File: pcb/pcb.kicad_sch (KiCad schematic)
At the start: 121 parts, among them J1 Conn_01x06_Pin, SW1 SW_Push_45deg, SW10 SW_Push_45deg, SW11 SW_Push_45deg, SW12 SW_Push_45deg, SW13 SW_Push_45deg, SW14 SW_Push_45deg, SW15 SW_Push_45deg, SW16 SW_Push_45deg, SW17 SW_Push_45deg, SW18 SW_Push_45deg, SW19 SW_Push_45deg, SW2 SW_Push_45deg, SW20 SW_Push_45deg, SW21 SW_Push_45deg, SW22 SW_Push_45deg, SW23 SW_Push_45deg, SW24 SW_Push_45deg, SW25 SW_Push_45deg, SW26 SW_Push_45deg, SW27 SW_Push_45deg, SW28 SW_Push_45deg, SW29 SW_Push_45deg, SW3 SW_Push_45deg, SW30 SW_Push_45deg, SW31 SW_Push_45deg, SW32 SW_Push_45deg, SW33 SW_Push_45deg, SW34 SW_Push_45deg, SW35 SW_Push_45deg, SW36 SW_Push_45deg, SW37 SW_Push_45deg, SW38 SW_Push_45deg, SW39 SW_Push_45deg, SW4 SW_Push_45deg, SW40 SW_Push_45deg, SW41 SW_Push_45deg, SW42 SW_Push_45deg, SW43 SW_Push_45deg, SW44 SW_Push_45deg, SW45 SW_Push_45deg, SW46 SW_Push_45deg, SW47 SW_Push_45deg, SW48 SW_Push_45deg, SW49 SW_Push_45deg, SW5 SW_Push_45deg, SW50 SW_Push_45deg, SW51 SW_Push, SW52 SW_Push, SW6 SW_Push_45deg, SW7 SW_Push_45deg, SW8 SW_Push_45deg, SW9 SW_Push_45deg, U1 STM32U575RGTxQ

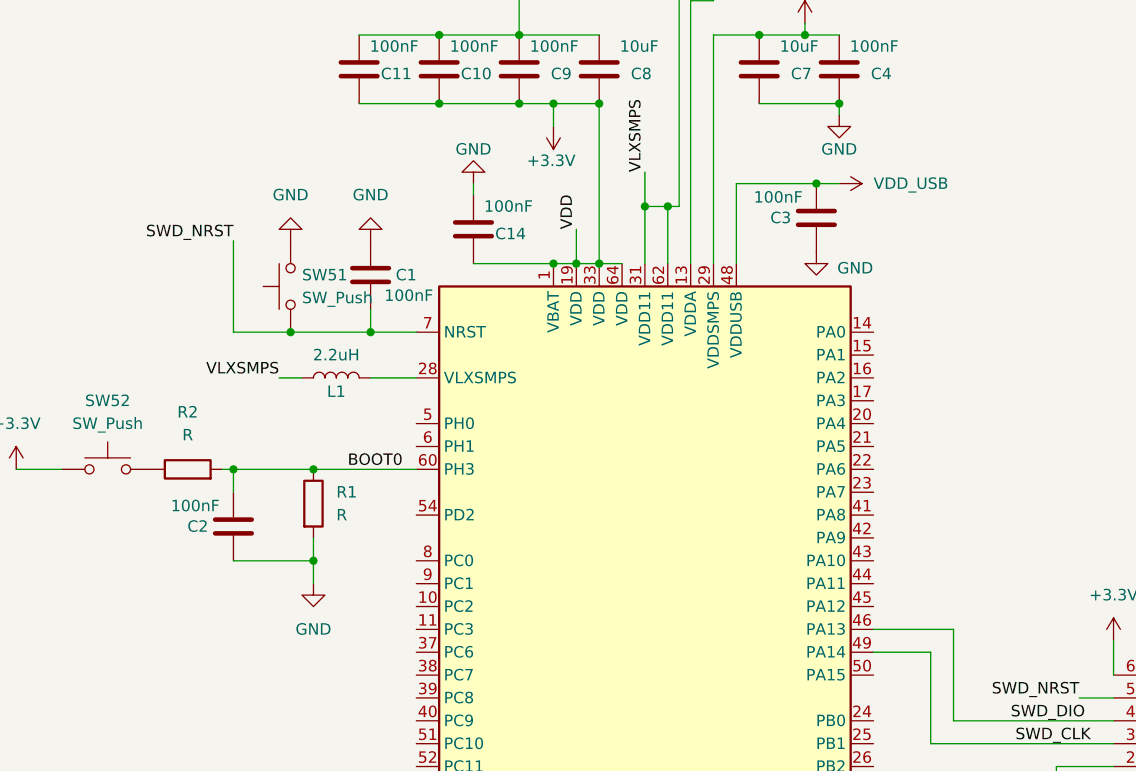
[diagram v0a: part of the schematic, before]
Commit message: [Hardware] Add R1 and R2 values, tied VDDUSB to VDD correctly
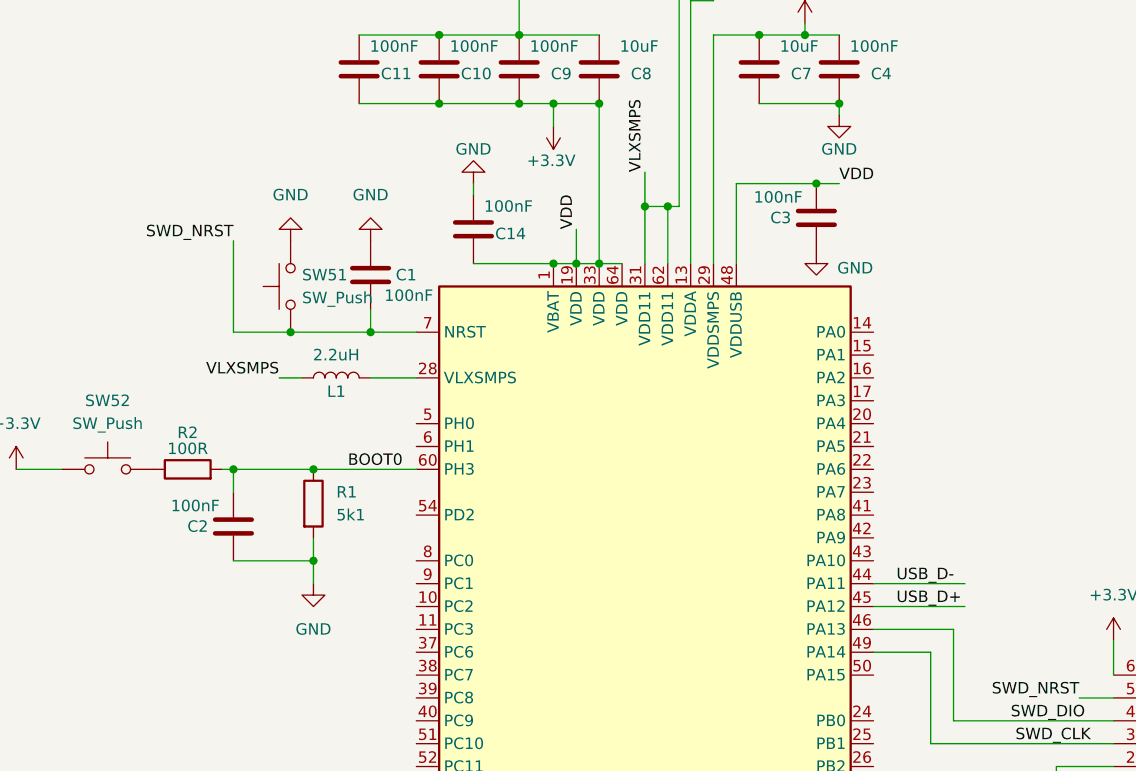
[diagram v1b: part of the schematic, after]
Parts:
- R1: value R -> 5k1
- R2: value R -> 100R
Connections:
- net VDD_USB is gone; now on net +3.3V: C3.2, U1.48 (VDDUSB)
- net USB_D-: now reaches U1.44 (PA11)
- net USB_D+: now reaches U1.45 (PA12)
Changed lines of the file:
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@@
 	(wire
 		(pts
+			(xy 226.06 148.59) (xy 236.22 148.59)
+		)
+		(stroke
+			(width 0)
+			(type default)
+		)
+	)
+	(wire
+		(pts
 			(xy 95.25 88.9) (xy 109.22 88.9)
 		)
@@
 	(wire
 		(pts
+			(xy 226.06 146.05) (xy 236.22 146.05)
+		)
+		(stroke
+			(width 0)
+			(type default)
+		)
+	)
+	(wire
+		(pts
 			(xy 24.13 195.58) (xy 39.37 195.58)
 		)
@@
 		)
 	)
+	(label "USB_D-"
+		(at 228.6 146.05 0)
+		(effects
+			(font
+				(size 1.27 1.27)
+			)
+			(justify left bottom)
+		)
+	)
 	(label "BOOT0"
 		(at 167.64 133.35 0)
@@
 		)
 	)
+	(label "USB_D+"
+		(at 228.6 148.59 0)
+		(effects
+			(font
+				(size 1.27 1.27)
+			)
+			(justify left bottom)
+		)
+	)
 	(label "VLXSMPS"
 		(at 160.02 123.19 180)
@@
 		)
 	)
+	(label "VDD"
+		(at 222.25 101.6 0)
+		(effects
+			(font
+				(size 1.27 1.27)
+			)
+			(justify left bottom)
+		)
+	)
 	(label "SWD_NRST"
 		(at 154.94 107.95 180)
@@
 			)
 		)
-		(property "Value" "R"
+		(property "Value" "5k1"
 			(at 166.37 138.4299 0)
 			(effects
@@
 	)
 	(symbol
-		(lib_id "power:VDD")
-		(at 222.25 101.6 270)
-		(unit 1)
-		(exclude_from_sim no)
-		(in_bom yes)
-		(on_board yes)
-		(dnp no)
-		(fields_autoplaced yes)
-		(property "Reference" "#PWR08"
-			(at 218.44 101.6 0)
-			(effects
-				(font
-					(size 1.27 1.27)
-				)
-				(hide yes)
-			)
-		)
-		(property "Value" "VDD_USB"
-			(at 226.06 101.5999 90)
-			(effects
-				(font
-					(size 1.27 1.27)
-				)
-				(justify left)
-			)
-		)
-		(property "Footprint" ""
-			(at 222.25 101.6 0)
-			(effects
-				(font
-					(size 1.27 1.27)
-				)
-				(hide yes)
-			)
-		)
-		(property "Datasheet" ""
-			(at 222.25 101.6 0)
-			(effects
-				(font
-					(size 1.27 1.27)
-				)
-				(hide yes)
-			)
-		)
-		(property "Description" "Power symbol creates a global label with name \"VDD\""
-			(at 222.25 101.6 0)
-			(effects
-				(font
-					(size 1.27 1.27)
-				)
-				(hide yes)
-			)
-		)
-		(pin "1"
-		)
-		(instances
-			(project ""
-				(path "/f2ec7380-d5e2-4be5-b548-cc5c4c4a2ed6"
-					(reference "#PWR08")
-					(unit 1)
-				)
-			)
-		)
-	)
-	(symbol
 		(lib_id "Switch:SW_Push_45deg")
 		(at 106.68 100.33 0)
@@
 		(on_board yes)
 		(dnp no)
-		(fields_autoplaced yes)
 		(property "Reference" "R2"
-			(at 149.86 127 90)
+			(at 149.86 129.286 90)
 			(effects
 				(font
@@
 			)
 		)
-		(property "Value" "R"
-			(at 149.86 129.54 90)
+		(property "Value" "100R"
+			(at 149.86 131.064 90)
 			(effects
 				(font

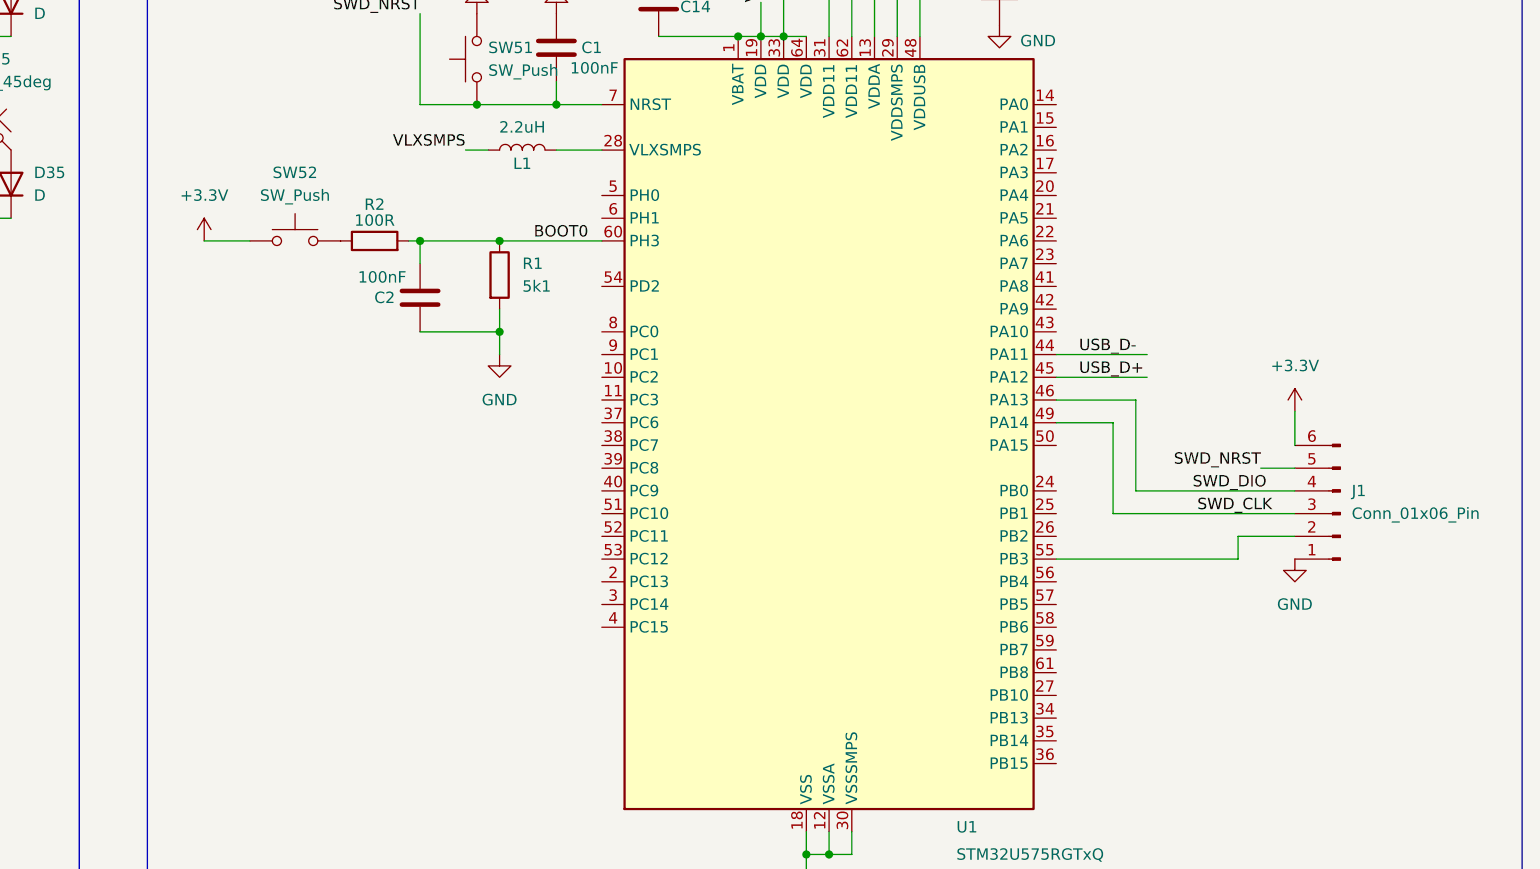
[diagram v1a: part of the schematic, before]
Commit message: [Hardware] Add keyboard pin mapping to MCU
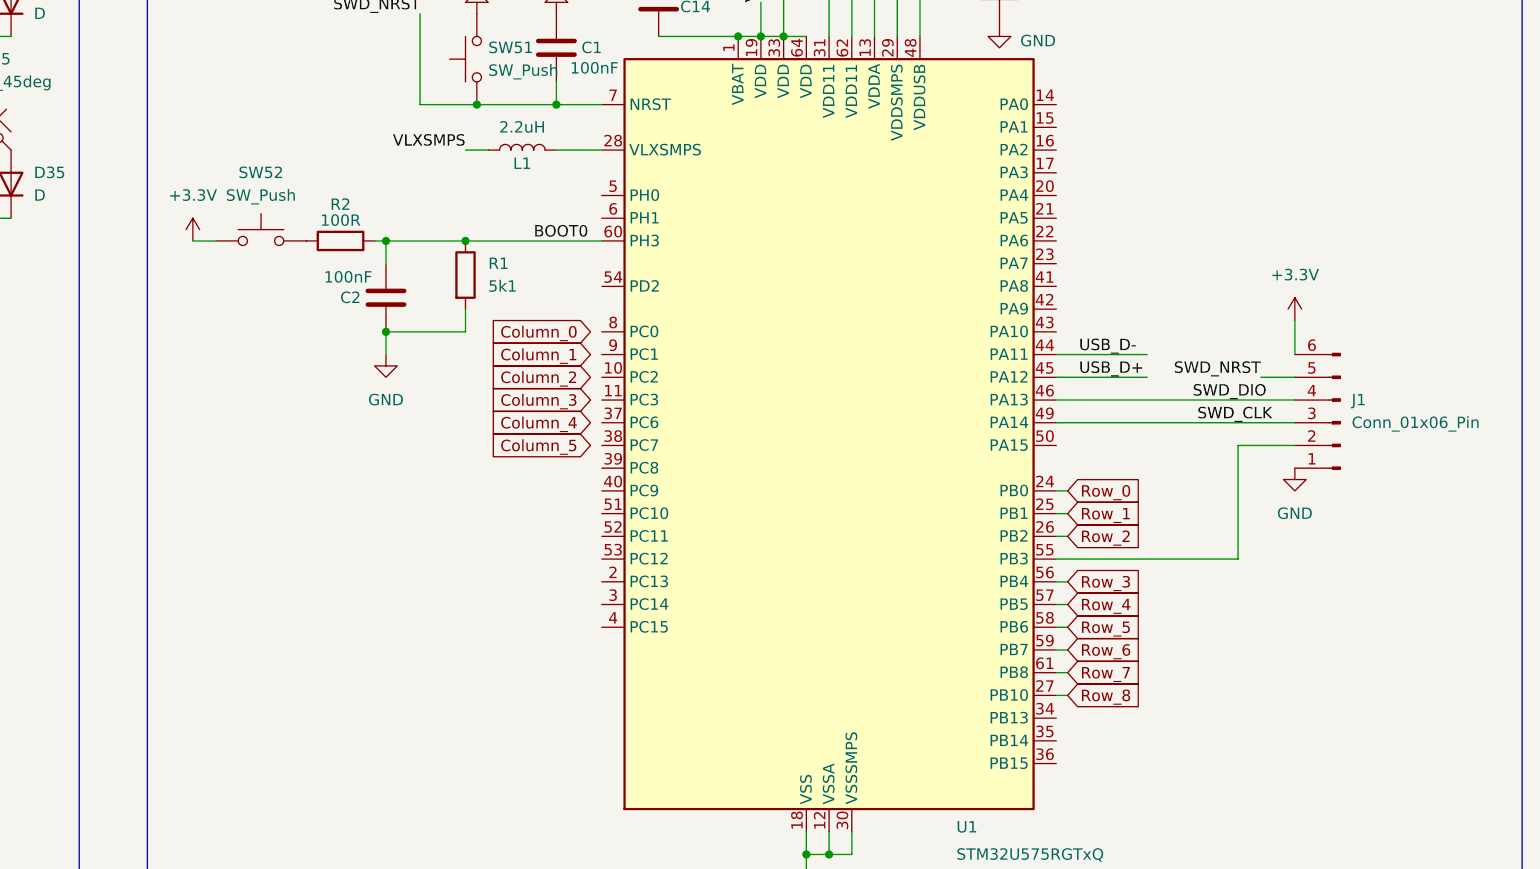
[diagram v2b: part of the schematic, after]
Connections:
- net Row_0: now also U1.24 (PB0)
- net Row_1: now also U1.25 (PB1)
- net Row_2: now also U1.26 (PB2)
- net Row_3: now also U1.56 (PB4)
- net Row_4: now also U1.57 (PB5)
- net Row_5: now also U1.58 (PB6)
- net Row_6: now also U1.59 (PB7)
- net Row_7: now also U1.61 (PB8)
- net Row_8: now also U1.27 (PB10)
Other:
- moved on the sheet: C2, J1, R1, R2, SW52
